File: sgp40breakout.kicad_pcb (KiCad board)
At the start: 2 copper layers, 15 x 11.2 mm, 14 parts, among them J1 Conn_01x04_Male, U1 SGP40, U2 SHT35-DIS

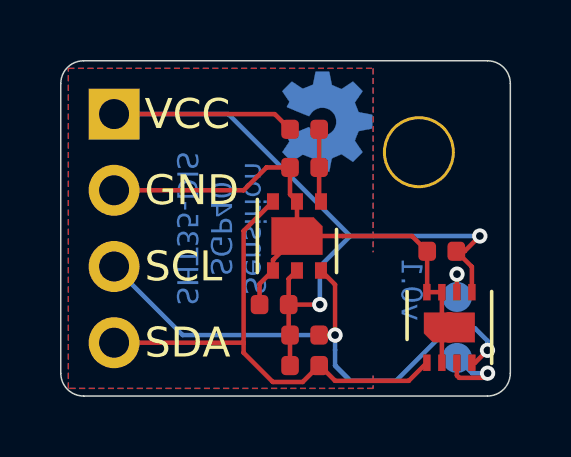
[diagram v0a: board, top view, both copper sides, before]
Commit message: increase milling slit to 5mm
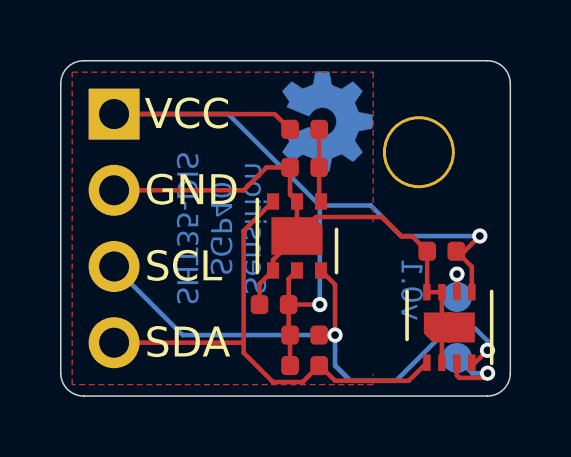
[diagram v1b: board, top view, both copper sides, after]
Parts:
- REF**: value DrillSlot_4mm -> DrillSlot_5mm; footprint sgp40breakout:DrillSlot_4mm -> sgp40breakout:DrillSlot_5mm
- moved REF** 0.44 mm to (134.4, 82.4)
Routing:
- net VCC: track 29.6 -> 30.1 mm
- net GND: track 20.5 -> 21.0 mm
- removed copper zone on B.Cu, net GND
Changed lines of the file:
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@@
     (thickness 1.6002)
     (drawings 14)
-    (tracks 88)
+    (tracks 91)
     (zones 0)
     (modules 14)
@@
     (add_net SDA)
     (add_net VCC)
+  )
+  (module sgp40breakout:DrillSlot_5mm (layer F.Cu)
+    (at 134.366 82.3595)
+    (fp_text reference REF** (at 0 0.5) (layer F.SilkS) hide
+      (effects (font (size 1 1) (thickness 0.15)))
+    )
+    (fp_text value DrillSlot_5mm (at 0 -0.5) (layer F.Fab) hide
+      (effects (font (size 1 1) (thickness 0.15)))
+    )
+    (pad "" np_thru_hole oval (at 0 0 180) (size 1 5) (drill oval 1 5) (layers *.Cu *.Mask))
   )
   (module sgp40breakout:OSHW-Symbol_3.3x3mm_Copper (layer B.Cu)
@@
     )
   )
-  (module sgp40breakout:DrillSlot_4mm (layer F.Cu)
-    (at 134.366 82.804)
-    (fp_text reference REF** (at 0 0.5) (layer F.SilkS) hide
-      (effects (font (size 1 1) (thickness 0.15)))
-    )
-    (fp_text value DrillSlot_4mm (at 0 -0.5) (layer F.Fab) hide
-      (effects (font (size 1 1) (thickness 0.15)))
-    )
-    (pad "" np_thru_hole oval (at 0 0 180) (size 1 4) (drill oval 1 4) (layers *.Cu *.Mask))
-  )
   (module Connector_PinHeader_2.54mm:PinHeader_1x04_P2.54mm_Vertical (layer B.Cu)
     (at 125.73 76.2 180)
@@
     (descr "Mounting Hole 2.2mm, M2")
     (tags "mounting hole 2.2mm m2")
+    (clearance 1.016)
     (attr virtual)
     (fp_text reference H1 (at 0 -3.2) (layer F.SilkS) hide
@@
   (segment (start 136.167 82.126) (end 136.156 82.137) (width 0.1524) (layer F.Cu) (net 1))
   (segment (start 136.167 80.772) (end 136.167 82.126) (width 0.1524) (layer F.Cu) (net 1))
-  (segment (start 135.659 80.264) (end 133.35 80.264) (width 0.1524) (layer F.Cu) (net 1))
-  (segment (start 136.167 80.772) (end 135.659 80.264) (width 0.1524) (layer F.Cu) (net 1))
   (segment (start 130.579 81.861) (end 131.026 81.414) (width 0.1524) (layer F.Cu) (net 1))
   (segment (start 130.579 82.55) (end 130.579 81.861) (width 0.1524) (layer F.Cu) (net 1))
   (segment (start 131.026 81.269378) (end 131.026 81.414) (width 0.1524) (layer F.Cu) (net 1))
-  (segment (start 133.35 80.264) (end 131.826 80.264) (width 0.1524) (layer F.Cu) (net 1))
   (segment (start 131.826 79.114) (end 131.826 80.264) (width 0.1524) (layer F.Cu) (net 1))
   (segment (start 131.026 81.064) (end 131.826 80.264) (width 0.1524) (layer F.Cu) (net 1))
@@
   (segment (start 130.81 77.978) (end 131.595 77.978) (width 0.1524) (layer F.Cu) (net 1))
   (segment (start 130.048 78.74) (end 130.81 77.978) (width 0.1524) (layer F.Cu) (net 1))
+  (segment (start 134.6678 79.63089) (end 135.3185 80.28159) (width 0.1524) (layer F.Cu) (net 1))
+  (segment (start 132.45911 79.63089) (end 134.6678 79.63089) (width 0.1524) (layer F.Cu) (net 1))
+  (segment (start 131.826 80.264) (end 132.45911 79.63089) (width 0.1524) (layer F.Cu) (net 1))
+  (segment (start 135.67659 80.28159) (end 136.167 80.772) (width 0.1524) (layer F.Cu) (net 1))
+  (segment (start 135.3185 80.28159) (end 135.67659 80.28159) (width 0.1524) (layer F.Cu) (net 1))
   (segment (start 132.565 76.708) (end 132.565 77.978) (width 0.1524) (layer F.Cu) (net 2))
   (segment (start 132.565 79.053) (end 132.626 79.114) (width 0.1524) (layer F.Cu) (net 2))
@@
   (segment (start 137.656 82.137) (end 137.656 81.291) (width 0.1524) (layer F.Cu) (net 3))
   (via (at 137.922 80.264) (size 0.508) (drill 0.254) (layers F.Cu B.Cu) (net 3))
-  (segment (start 137.414 80.772) (end 137.922 80.264) (width 0.1524) (layer F.Cu) (net 3))
-  (segment (start 137.137 80.772) (end 137.414 80.772) (width 0.1524) (layer F.Cu) (net 3))
   (via (at 132.588 82.55) (size 0.508) (drill 0.254) (layers F.Cu B.Cu) (net 3))
   (segment (start 132.588 82.55) (end 131.549 82.55) (width 0.1524) (layer F.Cu) (net 3))
@@
   (segment (start 131.549 82.55) (end 131.549 83.52) (width 0.1524) (layer F.Cu) (net 3))
   (segment (start 131.595 83.566) (end 131.595 84.582) (width 0.1524) (layer F.Cu) (net 3))
-  (segment (start 134.37559 80.264) (end 137.922 80.264) (width 0.1524) (layer B.Cu) (net 3))
-  (segment (start 133.604 80.264) (end 134.37559 80.264) (width 0.1524) (layer B.Cu) (net 3))
-  (segment (start 132.588 81.28) (end 133.604 80.264) (width 0.1524) (layer B.Cu) (net 3))
   (segment (start 132.588 82.55) (end 132.588 81.28) (width 0.1524) (layer B.Cu) (net 3))
   (segment (start 125.73 76.2) (end 131.064 76.2) (width 0.1524) (layer F.Cu) (net 3))
-  (segment (start 129.54 76.2) (end 133.604 80.264) (width 0.1524) (layer B.Cu) (net 3))
   (segment (start 125.73 76.2) (end 129.54 76.2) (width 0.1524) (layer B.Cu) (net 3))
+  (segment (start 132.588 81.28) (end 132.588 79.248) (width 0.1524) (layer B.Cu) (net 3))
+  (segment (start 129.54 76.2) (end 132.588 79.248) (width 0.1524) (layer B.Cu) (net 3))
+  (segment (start 135.30091 80.264) (end 137.922 80.264) (width 0.1524) (layer B.Cu) (net 3))
+  (segment (start 134.28491 79.248) (end 135.30091 80.264) (width 0.1524) (layer B.Cu) (net 3))
+  (segment (start 132.588 79.248) (end 134.28491 79.248) (width 0.1524) (layer B.Cu) (net 3))
+  (segment (start 137.414 80.772) (end 137.922 80.264) (width 0.1524) (layer F.Cu) (net 3))
+  (segment (start 137.137 80.772) (end 137.414 80.772) (width 0.1524) (layer F.Cu) (net 3))
   (via (at 133.096 83.566) (size 0.508) (drill 0.254) (layers F.Cu B.Cu) (net 4))
   (segment (start 132.565 83.566) (end 133.096 83.566) (width 0.1524) (layer F.Cu) (net 4))
@@
   (segment (start 137.668834 84.836834) (end 137.16 84.328) (width 0.1524) (layer B.Cu) (net 7))
   (segment (start 138.180453 84.836834) (end 137.668834 84.836834) (width 0.1524) (layer B.Cu) (net 7))
-  (zone (net 1) (net_name GND) (layer B.Cu) (hatch edge 0.508)
-    (connect_pads (clearance 0.1524))
-    (min_thickness 0.254)
-    (fill yes (arc_segments 32) (thermal_gap 0.508) (thermal_bridge_width 0.508) (smoothing fillet) (radius 0.762))
-    (polygon
-      (pts
-        (xy 134.366 85.344) (xy 124.206 85.344) (xy 124.206 74.676) (xy 134.366 74.676)
-      )
-    )
-  )
   (zone (net 1) (net_name GND) (layer F.Cu) (hatch edge 0.508)
     (connect_pads (clearance 0.1524))
     (min_thickness 0.254)
-    (fill yes (arc_segments 32) (thermal_gap 0.508) (thermal_bridge_width 0.508) (smoothing fillet) (radius 0.762))
+    (fill yes (arc_segments 32) (thermal_gap 0.3048) (thermal_bridge_width 0.3048) (smoothing fillet) (radius 0.762))
     (polygon
       (pts
-        (xy 134.366 85.344) (xy 124.206 85.344) (xy 124.206 74.676) (xy 134.366 74.676)
+        (xy 134.366 85.217) (xy 124.333 85.217) (xy 124.333 74.803) (xy 134.366 74.803)
       )
     )
